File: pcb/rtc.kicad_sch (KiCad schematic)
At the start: 8 parts, among them IC1 RV-3028-C7, SW1 SKRKAEE020

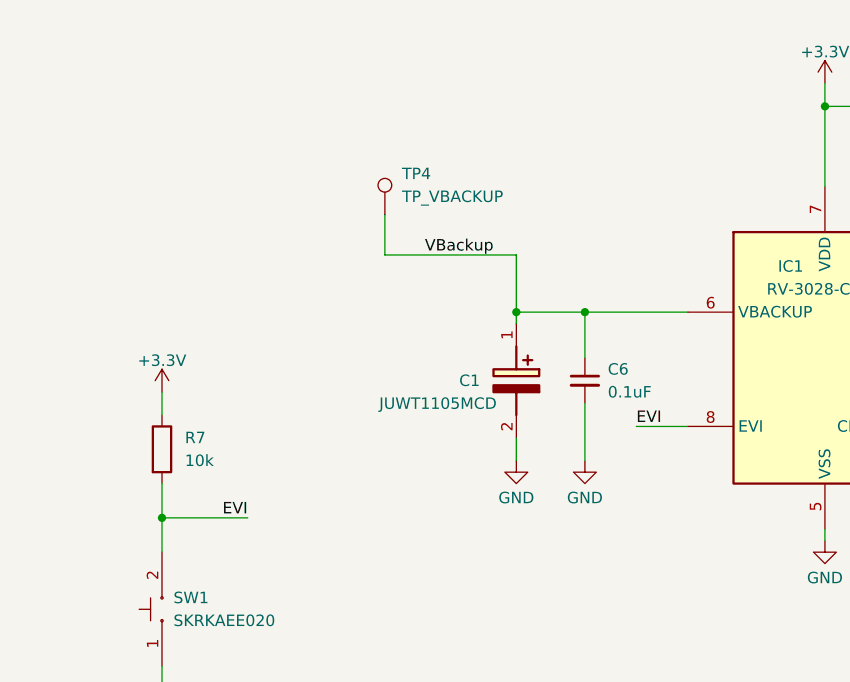
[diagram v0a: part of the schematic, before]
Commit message: Replaces nRF52840 with ESP32-S3
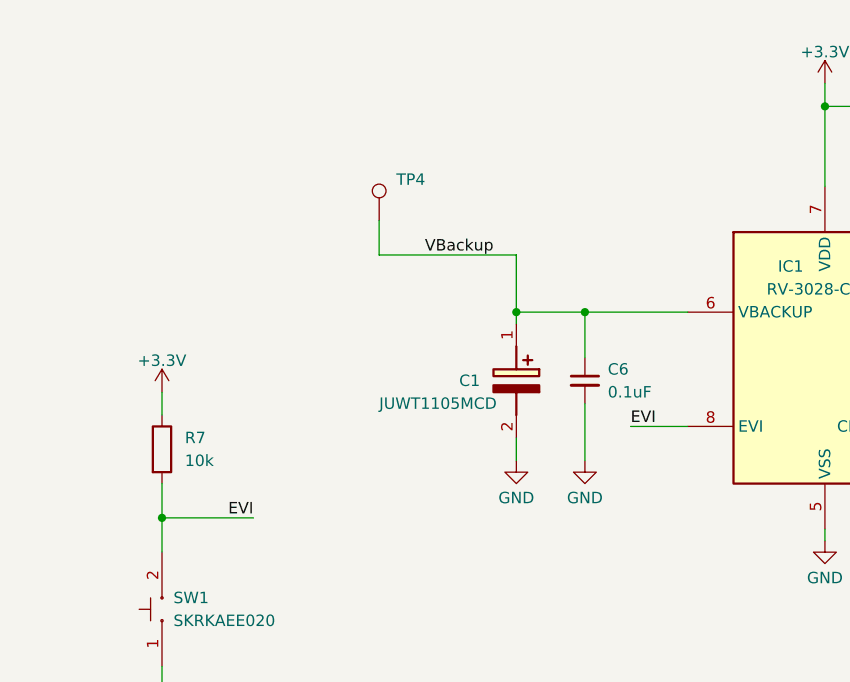
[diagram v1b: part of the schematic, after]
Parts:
- TP4: footprint TestPoint:TestPoint_Pad_D2.0mm -> TestPoint:TestPoint_Pad_D1.5mm
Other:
- moved on the sheet: TP4
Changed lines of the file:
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@@
     (stroke (width 0) (type default))
   )
-  (wire (pts (xy 98.425 86.36) (xy 113.03 86.36))
+  (wire (pts (xy 97.79 86.36) (xy 113.03 86.36))
     (stroke (width 0) (type default))
   )
@@
     (stroke (width 0) (type default))
   )
+  (wire (pts (xy 97.79 82.55) (xy 97.79 86.36))
+    (stroke (width 0) (type default))
+  )
   (wire (pts (xy 179.07 92.71) (xy 189.23 92.71))
     (stroke (width 0) (type default))
@@
     (stroke (width 0) (type default))
   )
-  (wire (pts (xy 126.365 105.41) (xy 132.08 105.41))
+  (wire (pts (xy 125.73 105.41) (xy 132.08 105.41))
     (stroke (width 0) (type default))
   )
@@
     (stroke (width 0) (type default))
   )
-  (wire (pts (xy 73.66 115.57) (xy 83.185 115.57))
+  (wire (pts (xy 73.66 115.57) (xy 83.82 115.57))
     (stroke (width 0) (type default))
   )
   (wire (pts (xy 73.66 115.57) (xy 73.66 119.38))
-    (stroke (width 0) (type default))
-  )
-  (wire (pts (xy 98.425 81.915) (xy 98.425 86.36))
     (stroke (width 0) (type default))
   )
@@
     (effects (font (size 1.27 1.27)) (justify left bottom))
   )
-  (label "EVI" (at 83.185 115.57 180) (fields_autoplaced)
+  (label "EVI" (at 83.82 115.57 180) (fields_autoplaced)
     (effects (font (size 1.27 1.27)) (justify right bottom))
   )
@@
     (effects (font (size 1.27 1.27)) (justify right bottom))
   )
-  (label "EVI" (at 126.365 105.41 0) (fields_autoplaced)
+  (label "EVI" (at 125.73 105.41 0) (fields_autoplaced)
     (effects (font (size 1.27 1.27)) (justify left bottom))
   )
@@
     )
   )
-  (symbol (lib_id "Connector:TestPoint") (at 98.425 81.915 0) (unit 1)
-    (in_bom no) (on_board yes) (dnp no) (fields_autoplaced)
-    (property "Reference" "TP4" (at 100.33 77.343 0)
+  (symbol (lib_id "Connector:TestPoint") (at 97.79 82.55 0) (unit 1)
+    (in_bom no) (on_board yes) (dnp no)
+    (property "Reference" "TP4" (at 99.695 77.978 0)
       (effects (font (size 1.27 1.27)) (justify left))
     )
-    (property "Value" "TP_VBACKUP" (at 100.33 79.883 0)
-      (effects (font (size 1.27 1.27)) (justify left))
-    )
-    (property "Footprint" "TestPoint:TestPoint_Pad_D2.0mm" (at 103.505 81.915 0)
-      (effects (font (size 1.27 1.27)) hide)
-    )
-    (property "Datasheet" "~" (at 103.505 81.915 0)
-      (effects (font (size 1.27 1.27)) hide)
-    )
+    (property "Value" "TP_VBACKUP" (at 97.79 81.153 0)
+      (effects (font (size 1.27 1.27)) (justify left) hide)
+    )
+    (property "Footprint" "TestPoint:TestPoint_Pad_D1.5mm" (at 102.87 82.55 0)
+      (effects (font (size 1.27 1.27)) hide)
+    )
+    (property "Datasheet" "~" (at 102.87 82.55 0)
+      (effects (font (size 1.27 1.27)) hide)
+    )

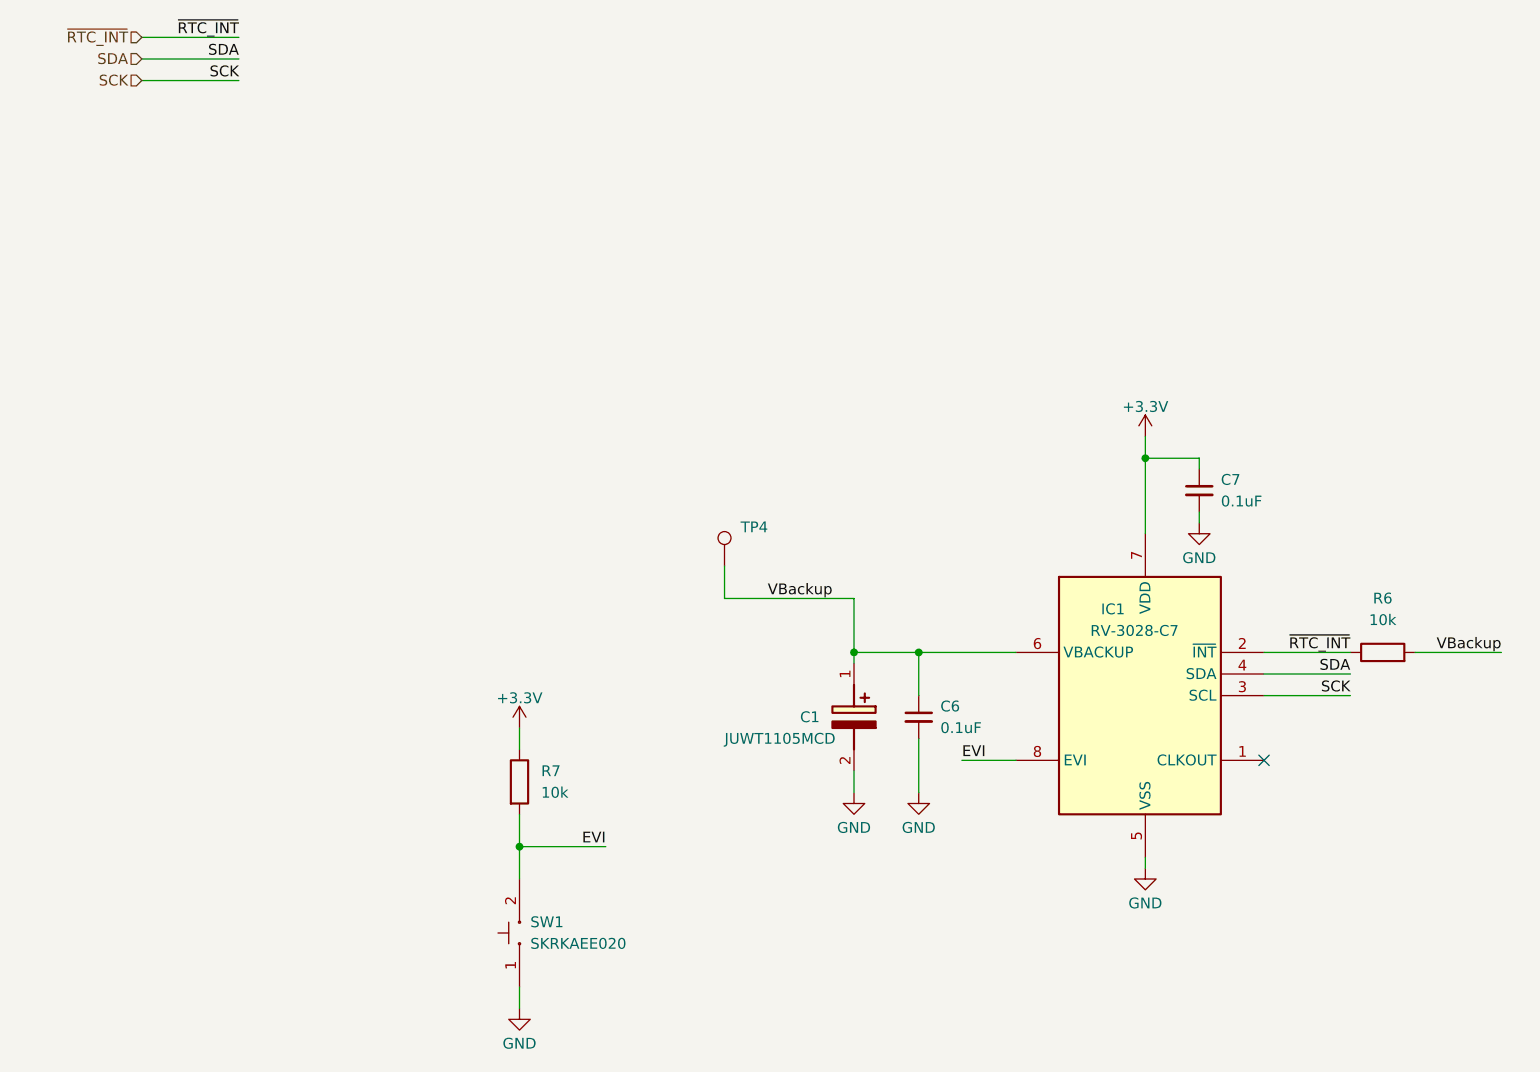
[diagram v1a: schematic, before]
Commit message: Refactored layout + silkscreen + added I2C connector
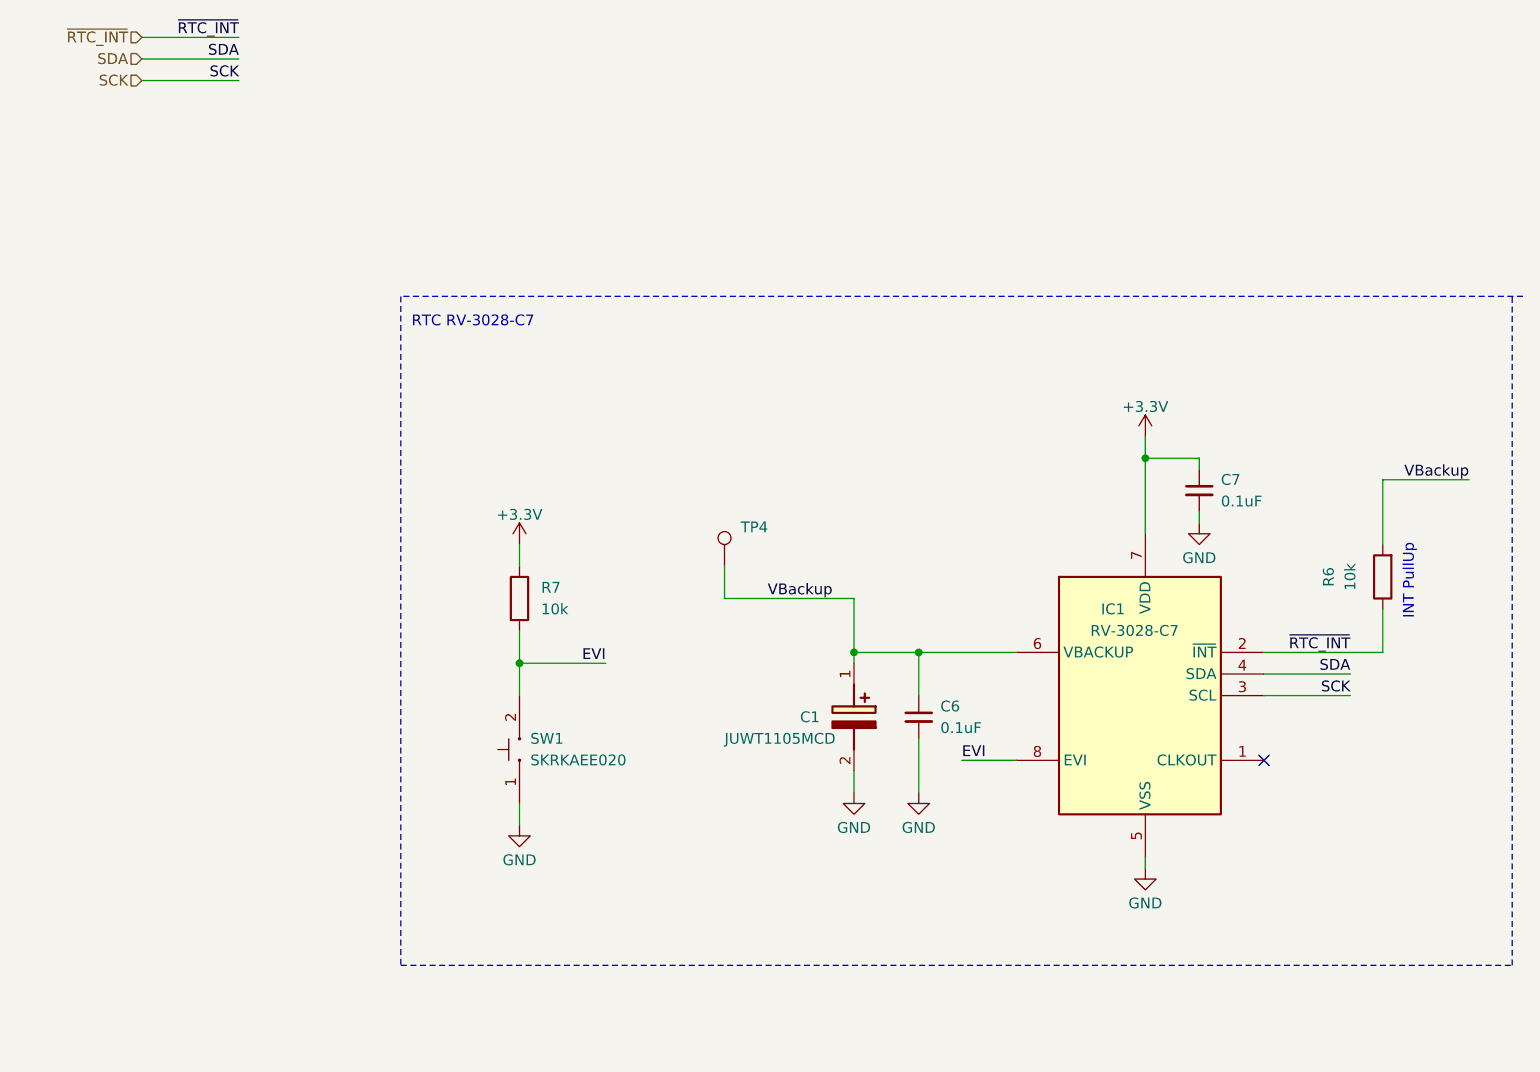
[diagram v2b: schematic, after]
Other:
- note added: "INT PullUp"
- note added: "RTC RV-3028-C7"
- moved on the sheet: R6, R7, SW1
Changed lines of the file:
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@@
   (junction (at 113.03 92.71) (diameter 0) (color 0 0 0 0)
   )
-  (junction (at 73.66 115.57) (diameter 0) (color 0 0 0 0)
+  (junction (at 73.66 93.98) (diameter 0) (color 0 0 0 0)
   )
   (junction (at 120.65 92.71) (diameter 0) (color 0 0 0 0)
@@
     (stroke (width 0) (type default))
   )
+  (wire (pts (xy 175.26 72.39) (xy 175.26 80.01))
+    (stroke (width 0) (type default))
+  )
   (wire (pts (xy 147.32 69.85) (xy 147.32 78.74))
     (stroke (width 0) (type default))
@@
     (stroke (width 0) (type default))
   )
+  (polyline (pts (xy 191.77 50.8) (xy 59.69 50.8))
+    (stroke (width 0) (type dash))
+  )
   (wire (pts (xy 113.03 106.68) (xy 113.03 109.22))
     (stroke (width 0) (type default))
@@
     (stroke (width 0) (type default))
   )
-  (wire (pts (xy 161.29 92.71) (xy 171.45 92.71))
+  (wire (pts (xy 161.29 92.71) (xy 175.26 92.71))
     (stroke (width 0) (type default))
   )
@@
     (stroke (width 0) (type default))
   )
+  (polyline (pts (xy 59.69 129.54) (xy 190.5 129.54))
+    (stroke (width 0) (type dash))
+  )
   (wire (pts (xy 120.65 92.71) (xy 113.03 92.71))
     (stroke (width 0) (type default))
@@
     (stroke (width 0) (type default))
   )
-  (wire (pts (xy 179.07 92.71) (xy 189.23 92.71))
+  (wire (pts (xy 175.26 72.39) (xy 185.42 72.39))
     (stroke (width 0) (type default))
   )
@@
     (stroke (width 0) (type default))
   )
-  (wire (pts (xy 73.66 132.08) (xy 73.66 134.62))
+  (polyline (pts (xy 190.5 129.54) (xy 190.5 50.8))
+    (stroke (width 0) (type dash))
+  )
+  (wire (pts (xy 73.66 110.49) (xy 73.66 113.03))
+    (stroke (width 0) (type default))
+  )
+  (polyline (pts (xy 59.69 50.8) (xy 59.69 129.54))
+    (stroke (width 0) (type dash))
+  )
+  (wire (pts (xy 175.26 87.63) (xy 175.26 92.71))
     (stroke (width 0) (type default))
   )
@@
     (stroke (width 0) (type default))
   )
-  (wire (pts (xy 73.66 111.76) (xy 73.66 115.57))
+  (wire (pts (xy 73.66 90.17) (xy 73.66 93.98))
     (stroke (width 0) (type default))
   )
@@
     (stroke (width 0) (type default))
   )
-  (wire (pts (xy 73.66 101.6) (xy 73.66 104.14))
-    (stroke (width 0) (type default))
-  )
-  (wire (pts (xy 73.66 115.57) (xy 83.82 115.57))
-    (stroke (width 0) (type default))
-  )
-  (wire (pts (xy 73.66 115.57) (xy 73.66 119.38))
-    (stroke (width 0) (type default))
+  (wire (pts (xy 73.66 80.01) (xy 73.66 82.55))
+    (stroke (width 0) (type default))
+  )
+  (wire (pts (xy 73.66 93.98) (xy 83.82 93.98))
+    (stroke (width 0) (type default))
+  )
+  (wire (pts (xy 73.66 93.98) (xy 73.66 97.79))
+    (stroke (width 0) (type default))
+  )
+  (text "INT PullUp" (at 179.07 88.9 90)
+    (effects (font (size 1.27 1.27)) (justify left bottom))
+  )
+  (text "RTC RV-3028-C7" (at 60.96 54.61 0)
+    (effects (font (size 1.27 1.27)) (justify left bottom))
   )
   (label "VBackup" (at 102.87 86.36 0) (fields_autoplaced)
     (effects (font (size 1.27 1.27)) (justify left bottom))
   )
-  (label "EVI" (at 83.82 115.57 180) (fields_autoplaced)
+  (label "EVI" (at 83.82 93.98 180) (fields_autoplaced)
     (effects (font (size 1.27 1.27)) (justify right bottom))
   )
@@
     (effects (font (size 1.27 1.27)) (justify right bottom))
   )
-  (label "VBackup" (at 189.23 92.71 180) (fields_autoplaced)
+  (label "VBackup" (at 185.42 72.39 180) (fields_autoplaced)
     (effects (font (size 1.27 1.27)) (justify right bottom))
   )
@@
     )
   )
-  (symbol (lib_id "power:+3.3V") (at 73.66 101.6 0) (unit 1)
-    (in_bom yes) (on_board yes) (dnp no) (fields_autoplaced)
-    (property "Reference" "#PWR034" (at 73.66 105.41 0)
-      (effects (font (size 1.27 1.27)) hide)
-    )
-    (property "Value" "+3.3V" (at 73.66 98.0981 0)
-      (effects (font (size 1.27 1.27)))
-    )
-    (property "Footprint" "" (at 73.66 101.6 0)
-      (effects (font (size 1.27 1.27)) hide)
-    )
-    (property "Datasheet" "" (at 73.66 101.6 0)
+  (symbol (lib_id "power:+3.3V") (at 73.66 80.01 0) (unit 1)
+    (in_bom yes) (on_board yes) (dnp no) (fields_autoplaced)
+    (property "Reference" "#PWR034" (at 73.66 83.82 0)
+      (effects (font (size 1.27 1.27)) hide)
+    )
+    (property "Value" "+3.3V" (at 73.66 76.5081 0)
+      (effects (font (size 1.27 1.27)))
+    )
+    (property "Footprint" "" (at 73.66 80.01 0)
+      (effects (font (size 1.27 1.27)) hide)
+    )
+    (property "Datasheet" "" (at 73.66 80.01 0)
       (effects (font (size 1.27 1.27)) hide)
     )
@@
     )
   )
-  (symbol (lib_id "Device:R") (at 175.26 92.71 90) (unit 1)
-    (in_bom yes) (on_board yes) (dnp no) (fields_autoplaced)
-    (property "Reference" "R6" (at 175.26 86.36 90)
-      (effects (font (size 1.27 1.27)))
-    )
-    (property "Value" "10k" (at 175.26 88.9 90)
-      (effects (font (size 1.27 1.27)))
-    )
-    (property "Footprint" "Resistor_SMD:R_0603_1608Metric" (at 175.26 94.488 90)
-      (effects (font (size 1.27 1.27)) hide)
-    )
-    (property "Datasheet" "~" (at 175.26 92.71 0)
+  (symbol (lib_id "Device:R") (at 175.26 83.82 180) (unit 1)
+    (in_bom yes) (on_board yes) (dnp no) (fields_autoplaced)
+    (property "Reference" "R6" (at 168.91 83.82 90)
+      (effects (font (size 1.27 1.27)))
+    )
+    (property "Value" "10k" (at 171.45 83.82 90)
+      (effects (font (size 1.27 1.27)))
+    )
+    (property "Footprint" "Resistor_SMD:R_0603_1608Metric" (at 177.038 83.82 90)
+      (effects (font (size 1.27 1.27)) hide)
+    )
+    (property "Datasheet" "~" (at 175.26 83.82 0)
       (effects (font (size 1.27 1.27)) hide)
     )
@@
     )
   )
-  (symbol (lib_id "Device:R") (at 73.66 107.95 0) (unit 1)
-    (in_bom yes) (on_board yes) (dnp no) (fields_autoplaced)
-    (property "Reference" "R7" (at 76.2 106.68 0)
-      (effects (font (size 1.27 1.27)) (justify left))
-    )
-    (property "Value" "10k" (at 76.2 109.22 0)
-      (effects (font (size 1.27 1.27)) (justify left))
-    )
-    (property "Footprint" "Resistor_SMD:R_0603_1608Metric" (at 71.882 107.95 90)
-      (effects (font (size 1.27 1.27)) hide)
-    )
-    (property "Datasheet" "~" (at 73.66 107.95 0)
+  (symbol (lib_id "Device:R") (at 73.66 86.36 0) (unit 1)
+    (in_bom yes) (on_board yes) (dnp no) (fields_autoplaced)
+    (property "Reference" "R7" (at 76.2 85.09 0)
+      (effects (font (size 1.27 1.27)) (justify left))
+    )
+    (property "Value" "10k" (at 76.2 87.63 0)
+      (effects (font (size 1.27 1.27)) (justify left))
+    )
+    (property "Footprint" "Resistor_SMD:R_0603_1608Metric" (at 71.882 86.36 90)
+      (effects (font (size 1.27 1.27)) hide)
+    )
+    (property "Datasheet" "~" (at 73.66 86.36 0)
       (effects (font (size 1.27 1.27)) hide)
     )
@@
     )
   )
-  (symbol (lib_id "power:GND") (at 73.66 134.62 0) (unit 1)
-    (in_bom yes) (on_board yes) (dnp no) (fields_autoplaced)
-    (property "Reference" "#PWR033" (at 73.66 140.97 0)
-      (effects (font (size 1.27 1.27)) hide)
-    )
-    (property "Value" "GND" (at 73.66 138.7555 0)
-      (effects (font (size 1.27 1.27)))
-    )
-    (property "Footprint" "" (at 73.66 134.62 0)
-      (effects (font (size 1.27 1.27)) hide)
-    )
-    (property "Datasheet" "" (at 73.66 134.62 0)
+  (symbol (lib_id "power:GND") (at 73.66 113.03 0) (unit 1)
+    (in_bom yes) (on_board yes) (dnp no) (fields_autoplaced)
+    (property "Reference" "#PWR033" (at 73.66 119.38 0)
+      (effects (font (size 1.27 1.27)) hide)
+    )
+    (property "Value" "GND" (at 73.66 117.1655 0)
+      (effects (font (size 1.27 1.27)))
+    )
+    (property "Footprint" "" (at 73.66 113.03 0)
+      (effects (font (size 1.27 1.27)) hide)
+    )
+    (property "Datasheet" "" (at 73.66 113.03 0)
       (effects (font (size 1.27 1.27)) hide)
     )
@@
     )
   )
-  (symbol (lib_id "SKRKAEE020:SKRKAEE020") (at 73.66 125.73 90) (unit 1)
-    (in_bom yes) (on_board yes) (dnp no) (fields_autoplaced)
-    (property "Reference" "SW1" (at 74.93 124.46 90)
+  (symbol (lib_id "SKRKAEE020:SKRKAEE020") (at 73.66 104.14 90) (unit 1)
+    (in_bom yes) (on_board yes) (dnp no) (fields_autoplaced)
+    (property "Reference" "SW1" (at 74.93 102.87 90)
       (effects (font (size 1.27 1.27)) (justify right))
     )
-    (property "Value" "SKRKAEE020" (at 74.93 127 90)
+    (property "Value" "SKRKAEE020" (at 74.93 105.41 90)
       (effects (font (size 1.27 1.27)) (justify right))
     )
-    (property "Footprint" "SKRKAEE020:SKRKAEE020" (at 73.66 125.73 0)
-      (effects (font (size 1.27 1.27)) hide)
-    )
-    (property "Datasheet" "" (at 73.66 125.73 0)
-      (effects (font (size 1.27 1.27)) hide)
-    )
+    (property "Footprint" "SKRKAEE020:SKRKAEE020" (at 73.66 104.14 0)
+      (effects (font (size 1.27 1.27)) hide)
+    )
+    (property "Datasheet" "" (at 73.66 104.14 0)
+      (effects (font (size 1.27 1.27)) hide)
+    )
